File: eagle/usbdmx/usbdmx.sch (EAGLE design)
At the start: 34 parts, among them IC1 MAX3468CSA, IC2 MAX3468CSA, Q1 16MHz

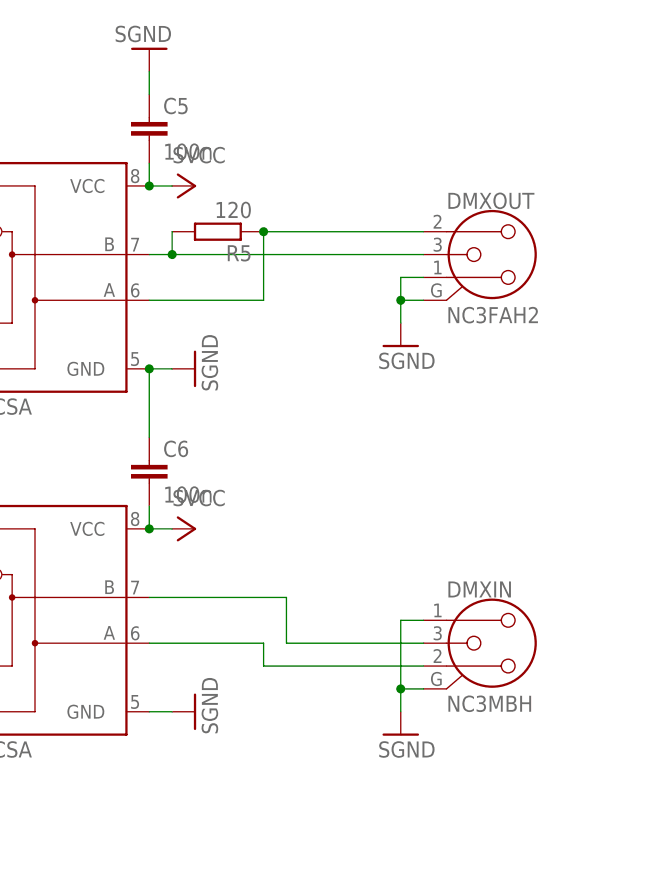
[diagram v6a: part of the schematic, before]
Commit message: make design smaller since the neutriks can be put closer
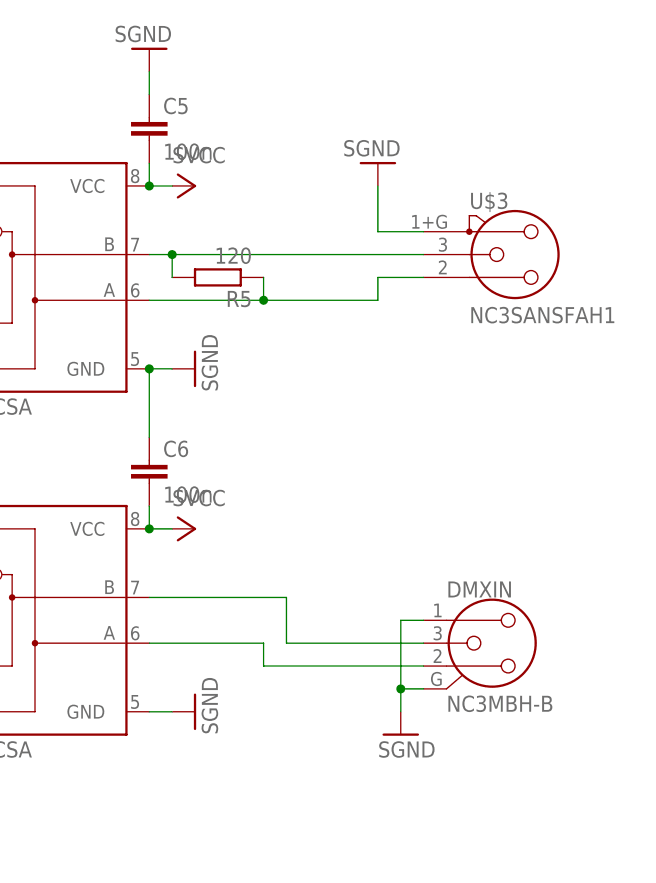
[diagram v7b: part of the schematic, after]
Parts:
- removed DMXOUT: NC3FAH2, con-neutrik_ag:NC3FAH2
- added U$3: NC3SANSFAH1, con-neutrik_ag:NC3SANSFAH1
- DMXIN: value NC3MBH -> NC3MBH-B; device con-neutrik_ag:NC3MBH -> con-neutrik_ag:NC3MBH-B
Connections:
- net N$12: now also U$3.2; no longer DMXOUT.1
- net N$17: now also U$3.3; no longer DMXOUT.3
- net SGND: now also U$3.1; no longer DMXOUT.2, DMXOUT.G
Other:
- moved on the sheet: R5
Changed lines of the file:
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@@
 <part name="P+7" library="supply1" deviceset="VCC" device=""/>
 <part name="C7" library="rcl" deviceset="C-EU" device="C0805" value="100n"/>
-<part name="DMXOUT" library="con-neutrik_ag" deviceset="NC3" device="FAH2"/>
-<part name="DMXIN" library="con-neutrik_ag" deviceset="NC3" device="MBH"/>
+<part name="DMXIN" library="con-neutrik_ag" deviceset="NC3" device="MBH-B" value="NC3MBH-B"/>
 <part name="U$2" library="murata-dcdc" deviceset="NTE0505S" device="NTE0505MEC"/>
 <part name="P+8" library="supply1" deviceset="VCC" device=""/>
@@
 <part name="GND8" library="supply1" deviceset="GND" device=""/>
 <part name="SJ1" library="jumper" deviceset="SJ" device=""/>
+<part name="U$3" library="con-neutrik_ag" deviceset="NC3SANS" device="FAH1"/>
 </parts>
 <sheets>
@@
 <instance part="P+7" gate="VCC" x="114.3" y="55.88" rot="R90"/>
 <instance part="C7" gate="G$1" x="27.94" y="73.66" rot="R90"/>
-<instance part="DMXOUT" gate="G$1" x="284.48" y="76.2"/>
 <instance part="DMXIN" gate="G$1" x="284.48" y="33.02"/>
 <instance part="U$2" gate="G$1" x="129.54" y="7.62"/>
@@
 <instance part="P+6" gate="VCC" x="251.46" y="83.82" rot="R270"/>
 <instance part="SGND4" gate="1" x="251.46" y="63.5" rot="R90"/>
-<instance part="SGND5" gate="1" x="274.32" y="66.04"/>
+<instance part="SGND5" gate="1" x="271.78" y="86.36" rot="R180"/>
 <instance part="C8" gate="G$1" x="144.78" y="7.62"/>
 <instance part="SGND6" gate="1" x="246.38" y="99.06" rot="R180"/>
-<instance part="R5" gate="G$1" x="254" y="78.74" rot="R180"/>
+<instance part="R5" gate="G$1" x="254" y="73.66" rot="R180"/>
 <instance part="OK1" gate="A" x="175.26" y="78.74"/>
 <instance part="OK2" gate="A" x="185.42" y="48.26" rot="R180"/>
@@
 <instance part="GND8" gate="1" x="116.84" y="73.66" rot="R90"/>
 <instance part="SJ1" gate="1" x="106.68" y="73.66" rot="R180"/>
+<instance part="U$3" gate="G$1" x="287.02" y="76.2"/>
 </instances>
 <busses>
@@
 <segment>
 <pinref part="IC2" gate="G$1" pin="B"/>
-<pinref part="DMXOUT" gate="G$1" pin="3"/>
 <wire x1="246.38" y1="76.2" x2="248.92" y2="76.2" width="0.1524" layer="91"/>
 <pinref part="R5" gate="G$1" pin="2"/>
-<wire x1="248.92" y1="76.2" x2="276.86" y2="76.2" width="0.1524" layer="91"/>
-<wire x1="248.92" y1="78.74" x2="248.92" y2="76.2" width="0.1524" layer="91"/>
+<wire x1="248.92" y1="73.66" x2="248.92" y2="76.2" width="0.1524" layer="91"/>
+<pinref part="U$3" gate="G$1" pin="3"/>
+<wire x1="276.86" y1="76.2" x2="248.92" y2="76.2" width="0.1524" layer="91"/>
 <junction x="248.92" y="76.2"/>
 </segment>
@@
 </segment>
 <segment>
-<wire x1="274.32" y1="68.58" x2="274.32" y2="71.12" width="0.1524" layer="91"/>
-<pinref part="DMXOUT" gate="G$1" pin="2"/>
-<wire x1="274.32" y1="71.12" x2="274.32" y2="73.66" width="0.1524" layer="91"/>
-<wire x1="274.32" y1="73.66" x2="276.86" y2="73.66" width="0.1524" layer="91"/>
-<pinref part="DMXOUT" gate="G$1" pin="G"/>
-<wire x1="276.86" y1="71.12" x2="274.32" y2="71.12" width="0.1524" layer="91"/>
-<junction x="274.32" y="71.12"/>
-<pinref part="SGND5" gate="1" pin="GND"/>
-</segment>
-<segment>
 <pinref part="C5" gate="G$1" pin="1"/>
 <pinref part="SGND6" gate="1" pin="GND"/>
@@
 <junction x="149.86" y="2.54"/>
 </segment>
+<segment>
+<pinref part="SGND5" gate="1" pin="GND"/>
+<wire x1="271.78" y1="83.82" x2="271.78" y2="78.74" width="0.1524" layer="91"/>
+<pinref part="U$3" gate="G$1" pin="1"/>
+<wire x1="271.78" y1="78.74" x2="276.86" y2="78.74" width="0.1524" layer="91"/>
+</segment>
 </net>
 <net name="N$20" class="0">
@@
 <net name="N$12" class="0">
 <segment>
-<wire x1="259.08" y1="71.12" x2="259.08" y2="78.74" width="0.1524" layer="91"/>
-<pinref part="DMXOUT" gate="G$1" pin="1"/>
-<wire x1="259.08" y1="78.74" x2="276.86" y2="78.74" width="0.1524" layer="91"/>
+<wire x1="259.08" y1="71.12" x2="259.08" y2="73.66" width="0.1524" layer="91"/>
 <pinref part="IC2" gate="G$1" pin="A"/>
 <wire x1="259.08" y1="71.12" x2="246.38" y2="71.12" width="0.1524" layer="91"/>
 <pinref part="R5" gate="G$1" pin="1"/>
-<junction x="259.08" y="78.74"/>
-</segment>
-</net>
+<wire x1="259.08" y1="71.12" x2="271.78" y2="71.12" width="0.1524" layer="91"/>
+<wire x1="271.78" y1="71.12" x2="271.78" y2="73.66" width="0.1524" layer="91"/>
+<junction x="259.08" y="71.12"/>
+<pinref part="U$3" gate="G$1" pin="2"/>
+<wire x1="271.78" y1="73.66" x2="276.86" y2="73.66" width="0.1524" layer="91"/>
+</segment>
+</net>

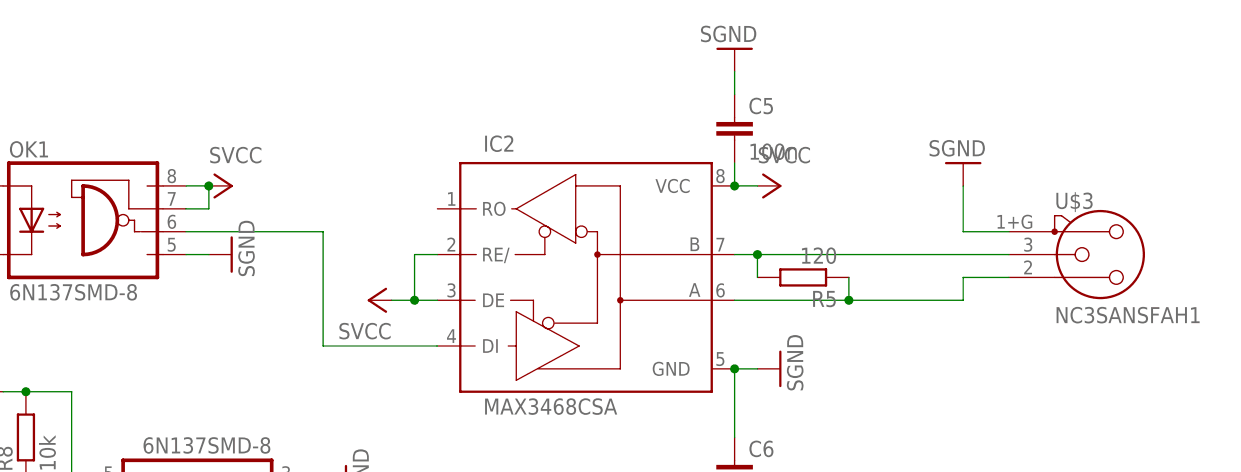
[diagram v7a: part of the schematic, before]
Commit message: add a necessary pull-up
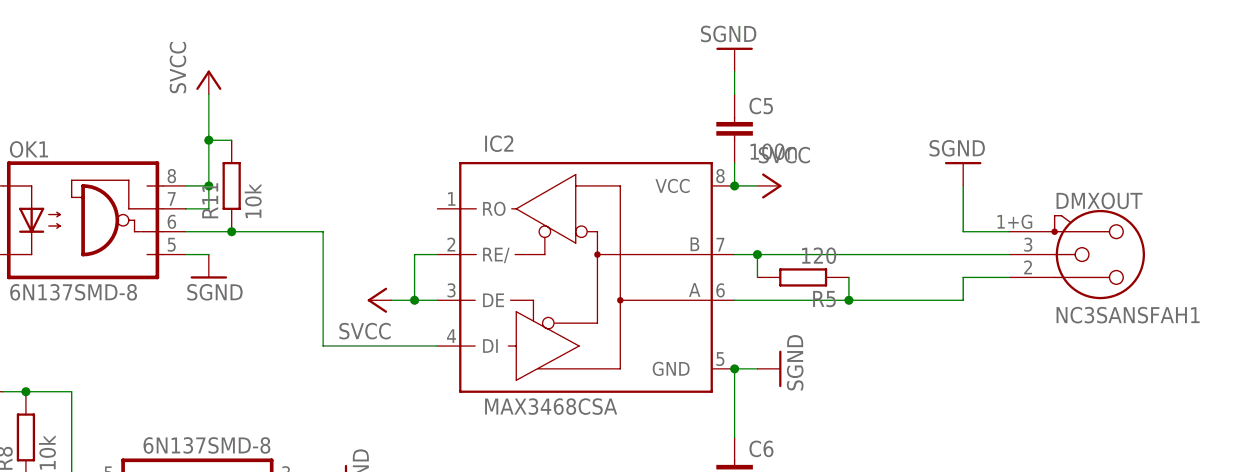
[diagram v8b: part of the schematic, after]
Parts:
- added R11: 10k, rcl:R-EU_R0805
- renumbered U$3 to DMXOUT
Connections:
- net N$20: now also R11.1
- net SVCC: now also R11.2
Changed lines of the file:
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@@
 <part name="GND8" library="supply1" deviceset="GND" device=""/>
 <part name="SJ1" library="jumper" deviceset="SJ" device=""/>
-<part name="U$3" library="con-neutrik_ag" deviceset="NC3SANS" device="FAH1"/>
+<part name="DMXOUT" library="con-neutrik_ag" deviceset="NC3SANS" device="FAH1"/>
+<part name="R11" library="rcl" deviceset="R-EU_" device="R0805" value="10k"/>
 </parts>
 <sheets>
@@
 <instance part="OK1" gate="A" x="175.26" y="78.74"/>
 <instance part="OK2" gate="A" x="185.42" y="48.26" rot="R180"/>
-<instance part="P+10" gate="VCC" x="190.5" y="83.82" rot="R270"/>
-<instance part="SGND7" gate="1" x="190.5" y="76.2" rot="R90"/>
+<instance part="P+10" gate="VCC" x="187.96" y="96.52"/>
+<instance part="SGND7" gate="1" x="187.96" y="73.66"/>
 <instance part="P+11" gate="VCC" x="170.18" y="43.18" rot="R90"/>
 <instance part="GND3" gate="1" x="162.56" y="60.96" rot="R270"/>
@@
 <instance part="GND8" gate="1" x="116.84" y="73.66" rot="R90"/>
 <instance part="SJ1" gate="1" x="106.68" y="73.66" rot="R180"/>
-<instance part="U$3" gate="G$1" x="287.02" y="76.2"/>
+<instance part="DMXOUT" gate="G$1" x="287.02" y="76.2"/>
+<instance part="R11" gate="G$1" x="190.5" y="83.82" rot="R90"/>
 </instances>
 <busses>
@@
 <pinref part="R5" gate="G$1" pin="2"/>
 <wire x1="248.92" y1="73.66" x2="248.92" y2="76.2" width="0.1524" layer="91"/>
-<pinref part="U$3" gate="G$1" pin="3"/>
+<pinref part="DMXOUT" gate="G$1" pin="3"/>
 <wire x1="276.86" y1="76.2" x2="248.92" y2="76.2" width="0.1524" layer="91"/>
 <junction x="248.92" y="76.2"/>
@@
 <segment>
 <pinref part="P+10" gate="VCC" pin="VCC"/>
-<pinref part="OK1" gate="A" pin="VCC"/>
-<wire x1="187.96" y1="83.82" x2="185.42" y2="83.82" width="0.1524" layer="91"/>
 <pinref part="OK1" gate="A" pin="VE"/>
 <wire x1="185.42" y1="81.28" x2="187.96" y2="81.28" width="0.1524" layer="91"/>
 <wire x1="187.96" y1="81.28" x2="187.96" y2="83.82" width="0.1524" layer="91"/>
+<pinref part="OK1" gate="A" pin="VCC"/>
+<wire x1="187.96" y1="83.82" x2="187.96" y2="88.9" width="0.1524" layer="91"/>
+<wire x1="187.96" y1="88.9" x2="187.96" y2="93.98" width="0.1524" layer="91"/>
+<wire x1="185.42" y1="83.82" x2="187.96" y2="83.82" width="0.1524" layer="91"/>
 <junction x="187.96" y="83.82"/>
+<pinref part="R11" gate="G$1" pin="2"/>
+<wire x1="190.5" y1="88.9" x2="187.96" y2="88.9" width="0.1524" layer="91"/>
+<junction x="187.96" y="88.9"/>
 </segment>
 </net>
@@
 <pinref part="SGND5" gate="1" pin="GND"/>
 <wire x1="271.78" y1="83.82" x2="271.78" y2="78.74" width="0.1524" layer="91"/>
-<pinref part="U$3" gate="G$1" pin="1"/>
+<pinref part="DMXOUT" gate="G$1" pin="1"/>
 <wire x1="271.78" y1="78.74" x2="276.86" y2="78.74" width="0.1524" layer="91"/>
 </segment>
@@
 <wire x1="213.36" y1="66.04" x2="200.66" y2="66.04" width="0.1524" layer="91"/>
 <pinref part="OK1" gate="A" pin="VO"/>
-<wire x1="185.42" y1="78.74" x2="200.66" y2="78.74" width="0.1524" layer="91"/>
+<wire x1="185.42" y1="78.74" x2="190.5" y2="78.74" width="0.1524" layer="91"/>
+<wire x1="190.5" y1="78.74" x2="200.66" y2="78.74" width="0.1524" layer="91"/>
 <wire x1="200.66" y1="78.74" x2="200.66" y2="66.04" width="0.1524" layer="91"/>
+<pinref part="R11" gate="G$1" pin="1"/>
+<junction x="190.5" y="78.74"/>
 </segment>
 </net>
@@
 <wire x1="271.78" y1="71.12" x2="271.78" y2="73.66" width="0.1524" layer="91"/>
 <junction x="259.08" y="71.12"/>
-<pinref part="U$3" gate="G$1" pin="2"/>
+<pinref part="DMXOUT" gate="G$1" pin="2"/>
 <wire x1="271.78" y1="73.66" x2="276.86" y2="73.66" width="0.1524" layer="91"/>
 </segment>
